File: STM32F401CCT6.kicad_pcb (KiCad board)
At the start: 2 copper layers, 52 x 23 mm, 43 parts, among them J1 USB_OTG, J2 Conn_02x03_Odd_Even, J3 Conn_01x20_des, J4 Conn_01x05_desc, J5 Conn_01x20, SW1 SW_Push, U1 MIC5219-3.3, U2 STM32F401CCT6, U3 USBLC6-2SC6, Y1 32.786K, Y2 8MHz

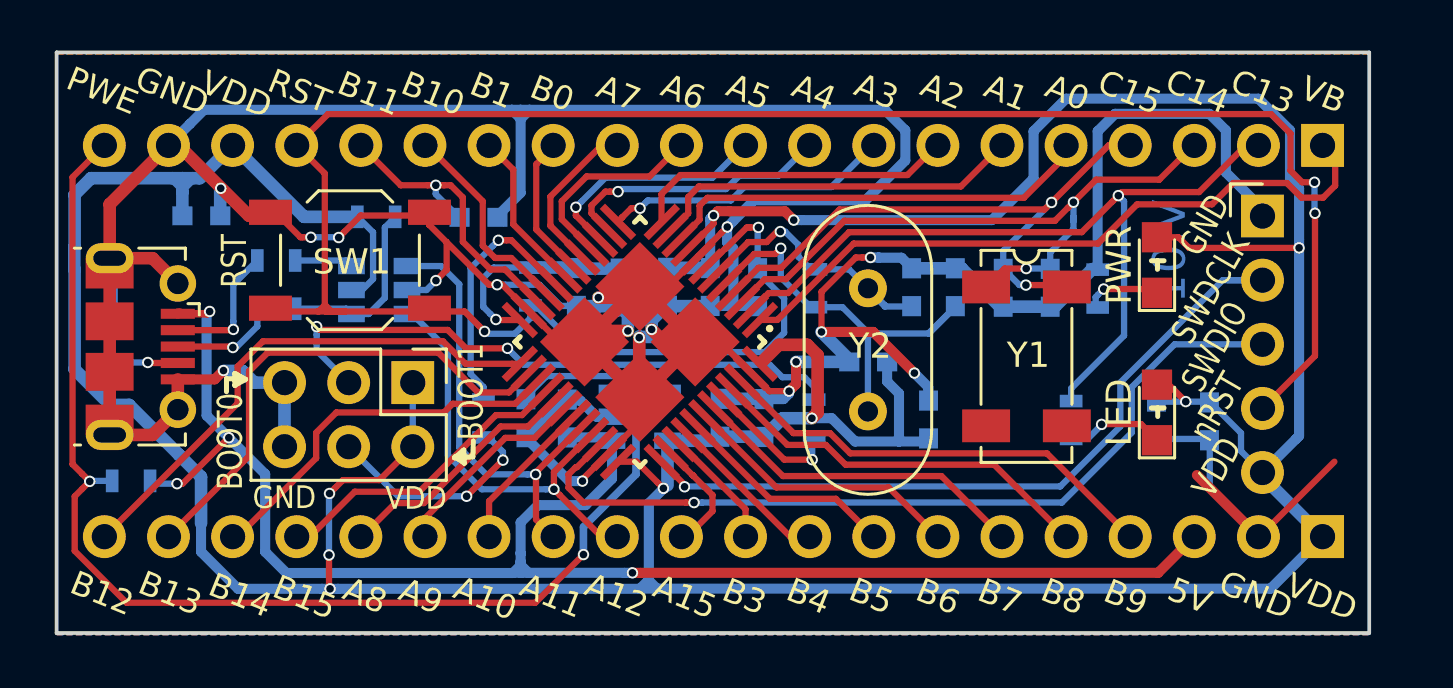
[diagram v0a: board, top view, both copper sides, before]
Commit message: Changed the 4 corner labels indication for footprint of QFN-QFP
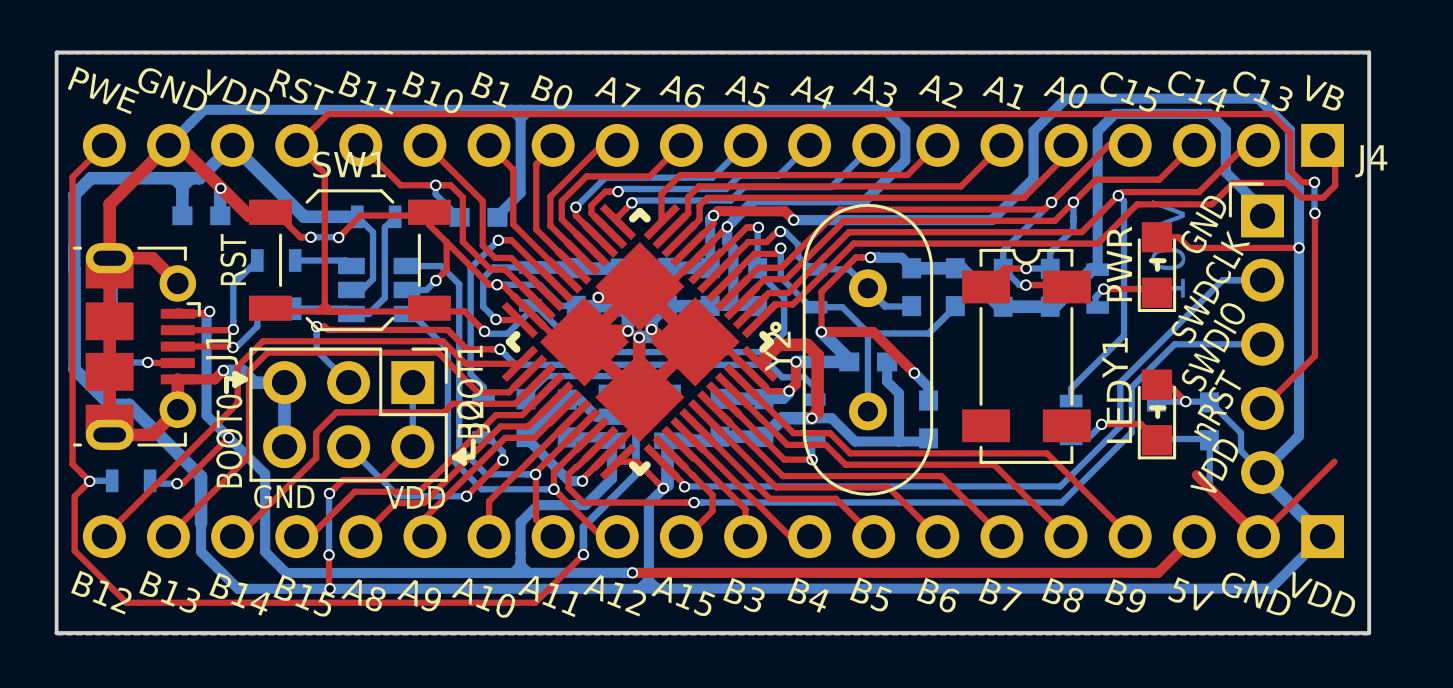
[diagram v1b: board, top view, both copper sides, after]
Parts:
- U2: footprint QFPN48:UFQFPN48 -> QFPN48:QFN_QFP48

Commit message: Found missing bottom silk layer, placed it back
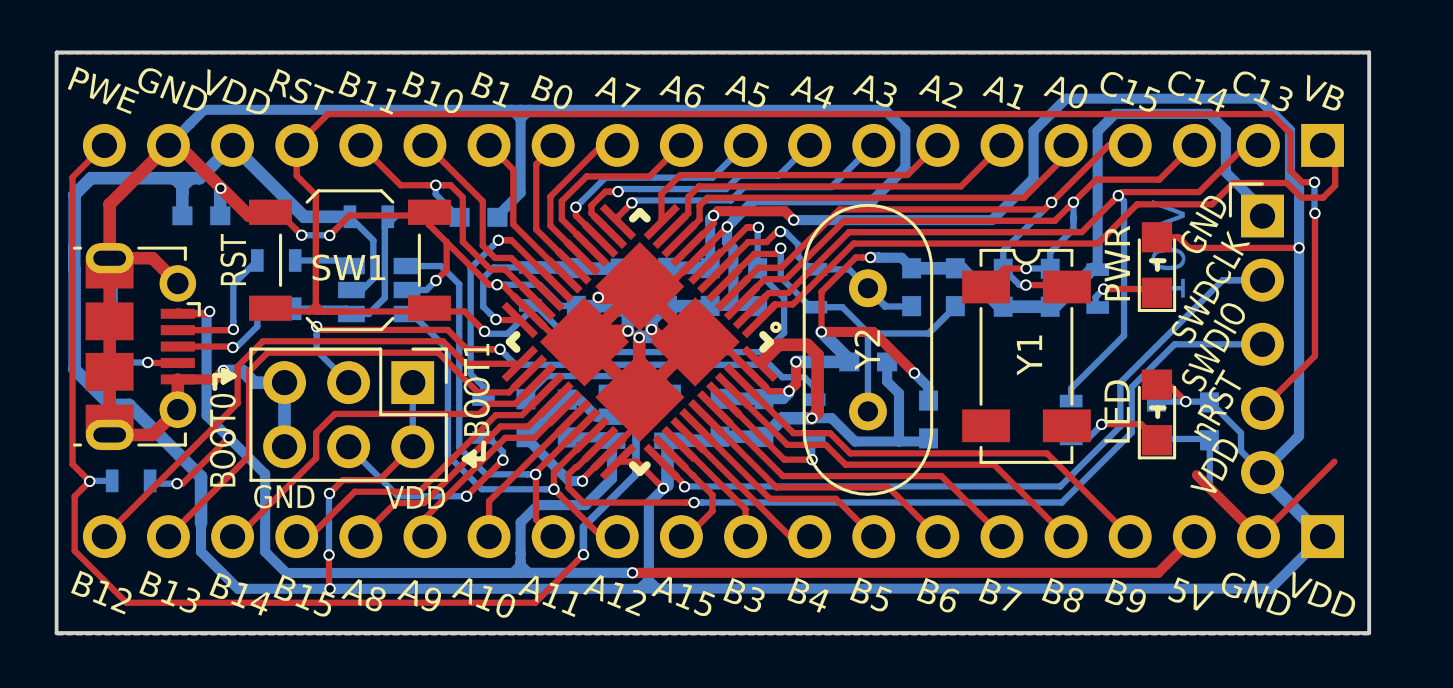
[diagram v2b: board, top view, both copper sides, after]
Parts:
- moved R10 0.29 mm to (49.0, 55.7)

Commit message: Enlarged the QFN-QFP48 footprint pin 1 indication label and the dimension label from 0.3mm to 0.4mm
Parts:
- U2: footprint QFPN48:QFN_QFP48 -> QFN_QFP48

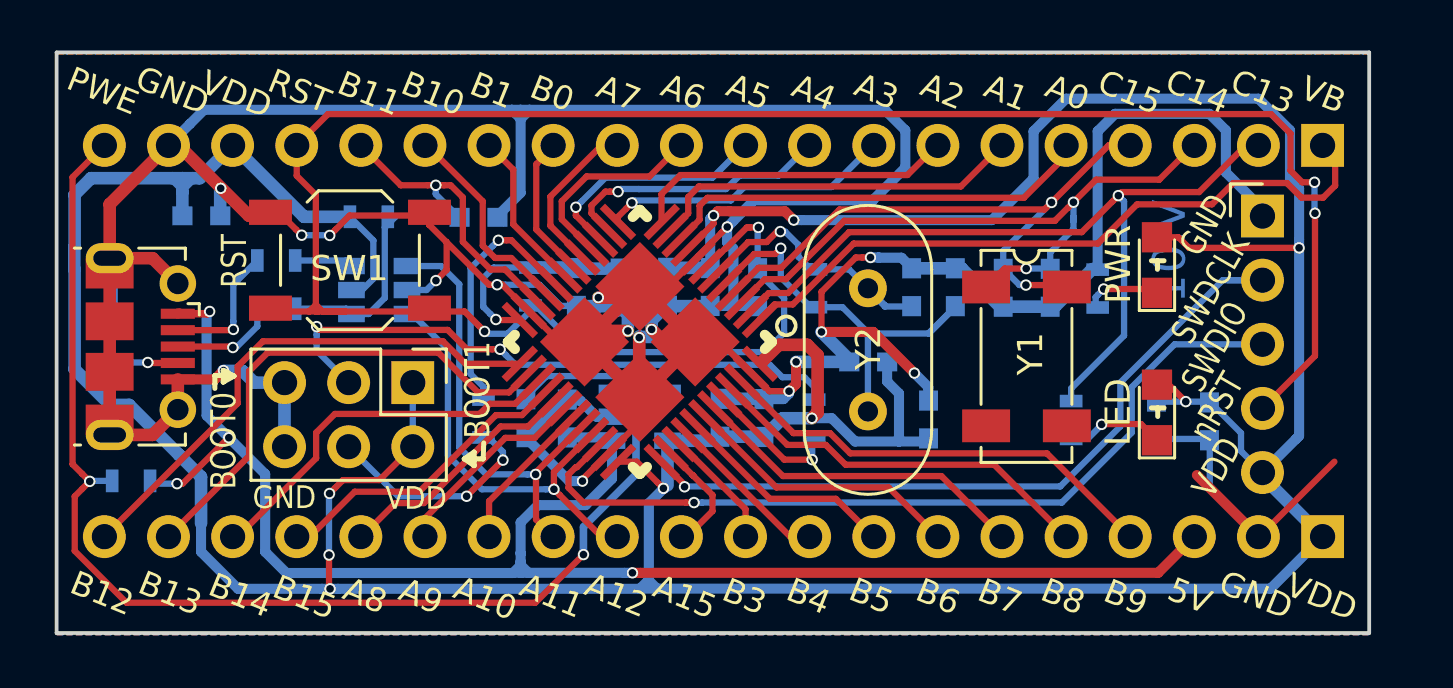
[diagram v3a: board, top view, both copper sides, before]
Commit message: Moved silk layer away from via and swap the position of VDD with nRST pin of the SWDIO
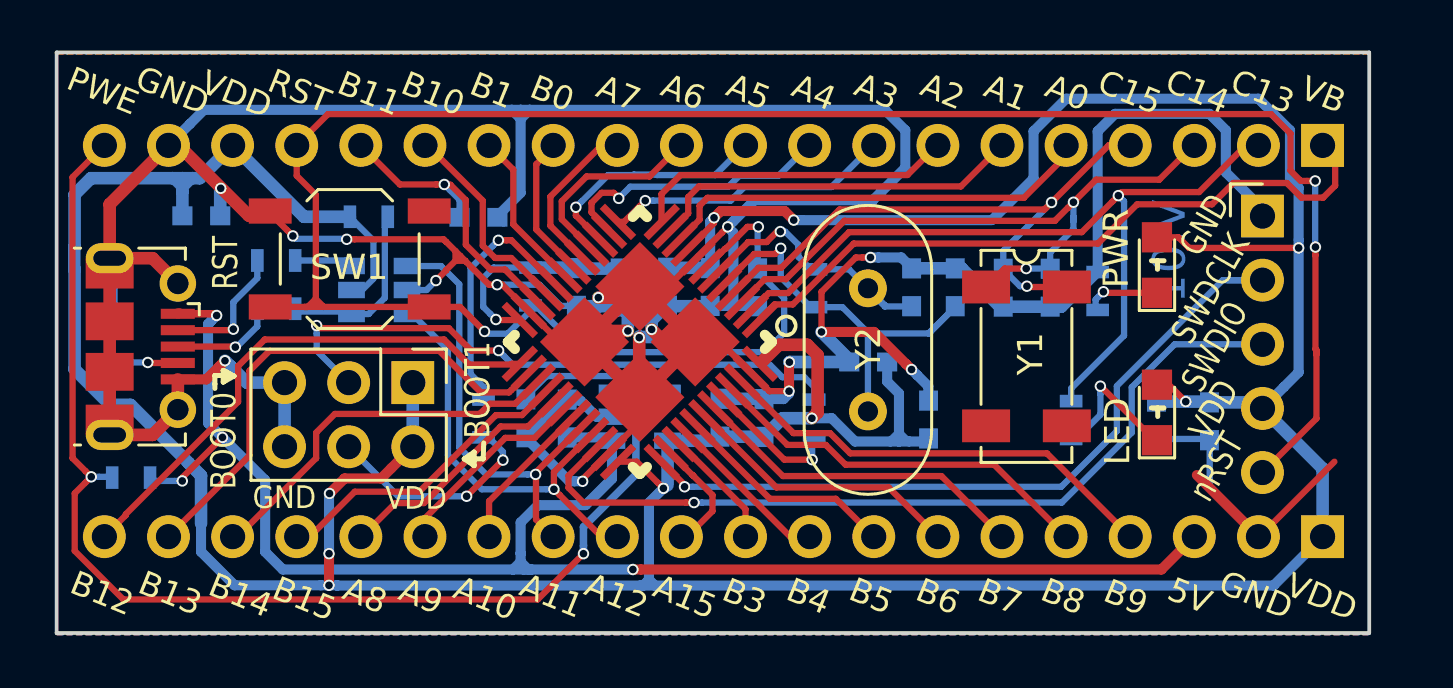
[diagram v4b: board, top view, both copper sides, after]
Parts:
- C1, C2: value 223,0603 -> 22n,0603
- C12, C13, C14, C17, C18, C5: value 104,0603 -> 0.1U,0603
- C3: value 105,0603 -> 1U,0603
- C4: value 106,0603 -> 10U,0603
- moved R11 0.13 mm to (39.5, 66.0)
- moved R5 0.10 mm to (77.8, 58.6)
- moved SW1 0.05 mm to (48.2, 57.4)
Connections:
- J4 pad 4: /RESET -> /VDD
- J4 pad 5: /VDD -> /RESET
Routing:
- net /RESET: track 91.3 -> 93.7 mm
- net /VDD: track 200.1 -> 198.0 mm
- net Net-(D2-Pad1): track 4.14 -> 6.03 mm
- net Net-(R10-Pad1): track 7.28 -> 6.69 mm
